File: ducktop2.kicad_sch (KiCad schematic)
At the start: 0 parts

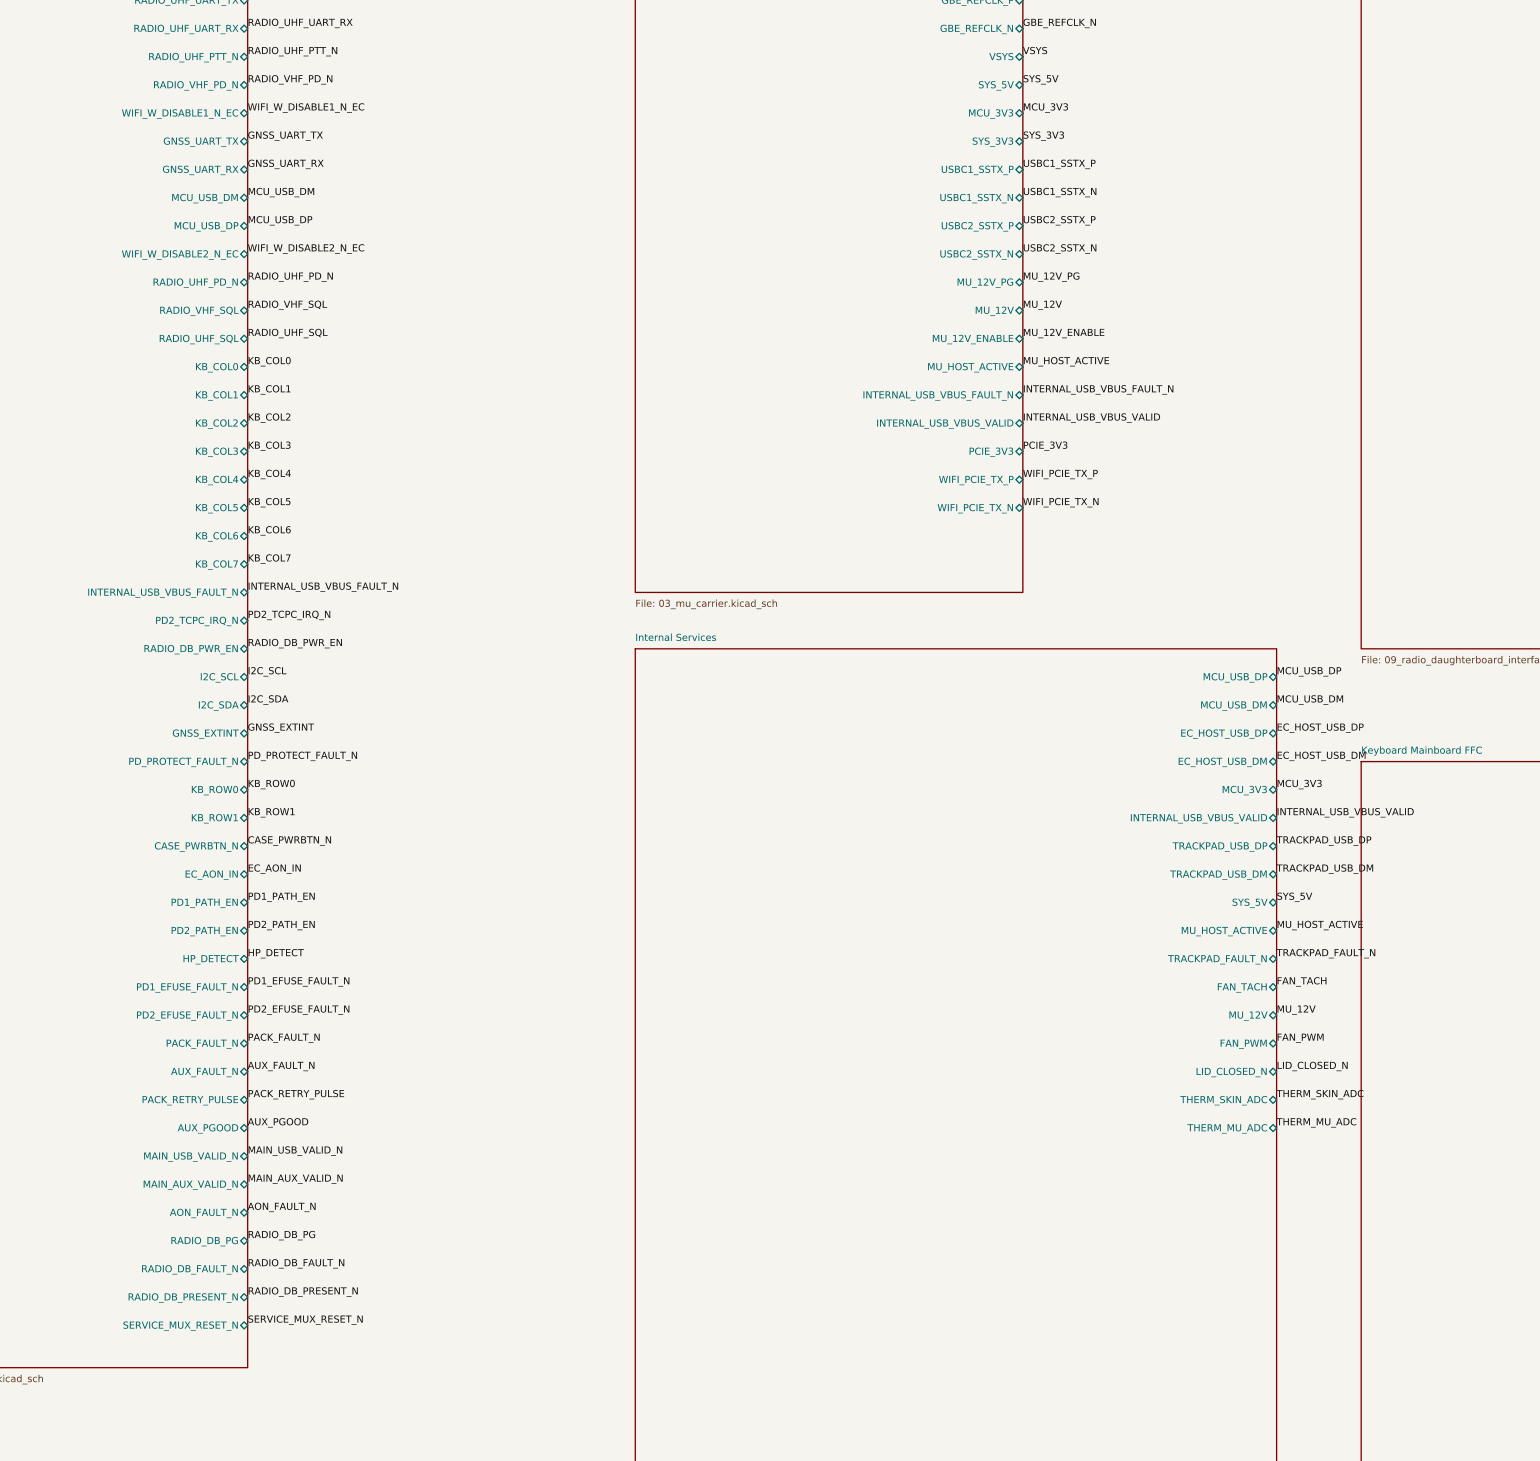
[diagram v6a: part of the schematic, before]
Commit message: Complete EC DFU port (J73) + DB power rework; verify schematic and board
- Add rear USB-C EC firmware programming port J73 (UFP/DFU) on Internal
  Services sheet: USBLC6-2P6 ESD (U63), 5.1k CC Rd resistors (R205/R211),
  22R series on D+/D- (R203/R204), mux-select hookup so BOOT0 high forces
  the USB mux to the DFU port
- Rename port ref J70->J73 after ham-radio collision; sync all net names
  (J73_CC1/J73_CC2)
- DB power rework: S5 gating + 3V3_STBY split, dual DCDC paths, GND
  returns on the standby rails; regenerate all sheets and re-verify
- sync_main_pcb_from_netlist: anchor placement for the 9 new footprints,
  scoped ECO support
- Board: rebuild main PCB with J73 footprint block (lib-sourced, net
  injection from netlist name attribute), sync pad nets for the 5 stale
  refs, remove duplicate R205/R211 copies
- Verified: check_schematic self-check OK (0 errors), radio DB contracts
  OK, ERC 0 errors, board DRC 0 electrical violations, board-vs-schematic
  net parity 0 conflicts, no duplicate refs
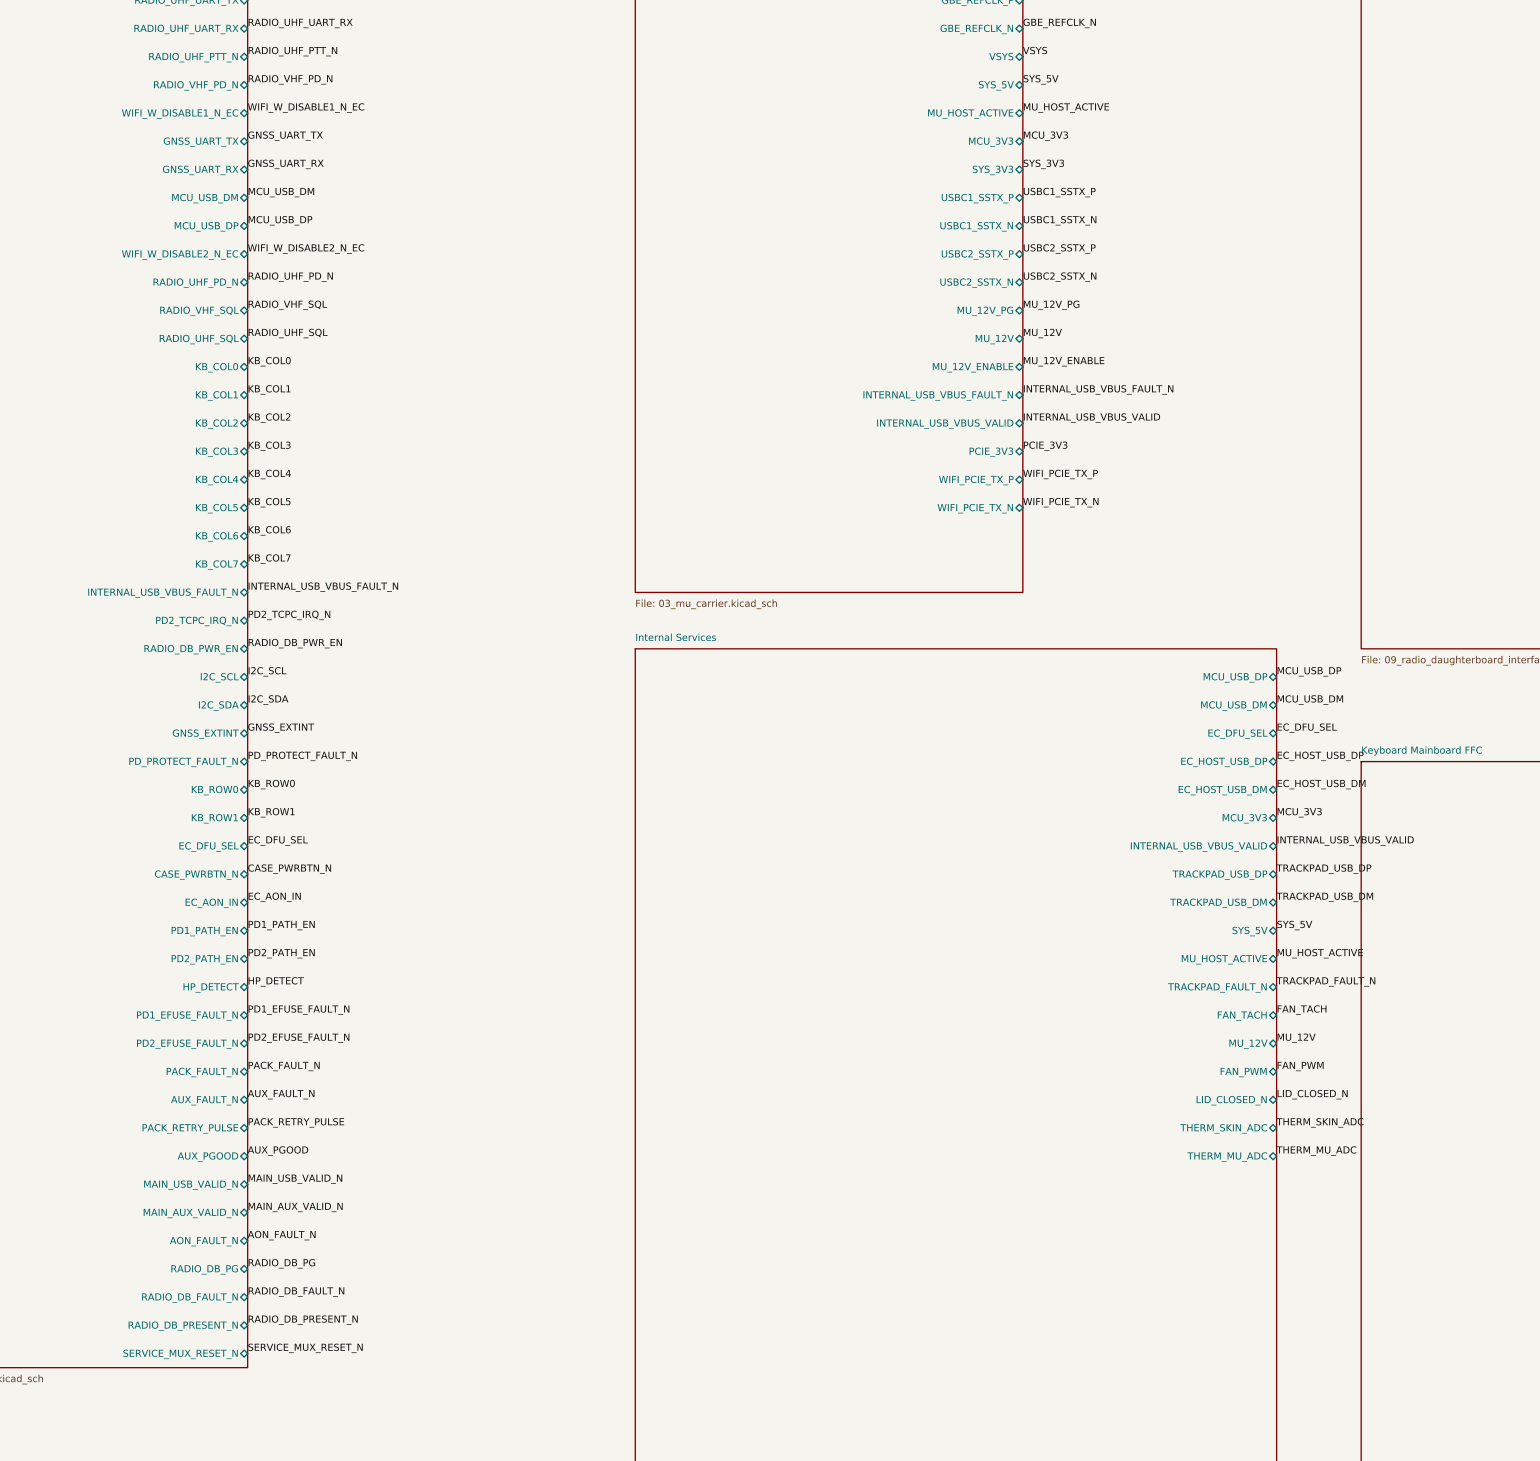
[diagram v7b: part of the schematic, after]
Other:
- sheet EC & MCU ports: added EC_DFU_SEL; removed none
- sheet Internal Services ports: added EC_DFU_SEL; removed none

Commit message: Close remaining electronics-review items: FAN1_TAC, SLS_S3, SIO UART, F5/F6
- P2-2: fan FG (FAN_TACH, 8.2k MCU_3V3 pull-up) now feeds Mu FAN1_TAC
  (A1 pin 4; SIO GP52 tach input per LattePanda-Mu pin tables) so the
  module's thermal policy sees real fan speed
- P3-2: Mu SLS_S3 (A1 pin 7; SoC GPD5, high in S0/S3 per Mu pin tables)
  observed on the TCA9539 spare input; R783 100k default-low pulldown so an
  absent Mu reads off
- P3-1: Mu SIO console (3.3V Super I/O UART, SIO JP3/GP41) exposed on
  on-board probe pads TP16/TP17 with 100k MCU_3V3 idle pull-ups (R779/R784)
  on the rear service edge; EC has no spare UART-capable pin (documented)
- F5: move H15 (240,70) -> (252,70) per retention doc (was under the Mu
  courtyard); move SW4/R212 on-board at (185/196,180) (were off-board at
  y=195/200); npth_inside_courtyard cleared
- F6: apply DIFF_85/90/100 + USB2_45 net classes with the impedance-doc
  geometries and project-default 0.15mm clearance (idempotent apply);
  include DFU_CONN/EC_DFU USB2 pairs in USB2_45
- F7: verified already released (commits 91c4f3b/caf6ffb documented the
  ethernet notch + mounting pattern as contracts)
- Root-sheet builder: auto-expand sheet blocks to fit their pin count
- Pin-review contracts updated for the new A1/U44 wiring
- Verified: check_schematic self-check OK, ERC 0 errors, radio DB contracts
  OK, board DRC 0 electrical violations (shorts/mask-bridges/npth all 0),
  board-vs-schematic net parity 0 conflicts
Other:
- sheet EC & MCU ports: added SLS_S3; removed none
- sheet Mu Carrier ports: added FAN_TACH, SLS_S3; removed none
